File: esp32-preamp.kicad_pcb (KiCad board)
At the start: 2 copper layers, 126 x 68 mm, 46 parts, among them J1 INPUT 1, J10 LFE, J11 OUT, J2 INPUT 2, J3 AMP PWR, J5 VOLUME, J6 TSOP382, J7 SELECT, J8 POT MOTOR, J9 PWR IN, Q1 2N3904, Q2 2N3904, Q3 2N3904, U3 TSR0.5-2450, U4 TLV702475DBV, U5 TPS60402DBV, U6 ESP32 D1 Mini, U7 TPS72301DBV

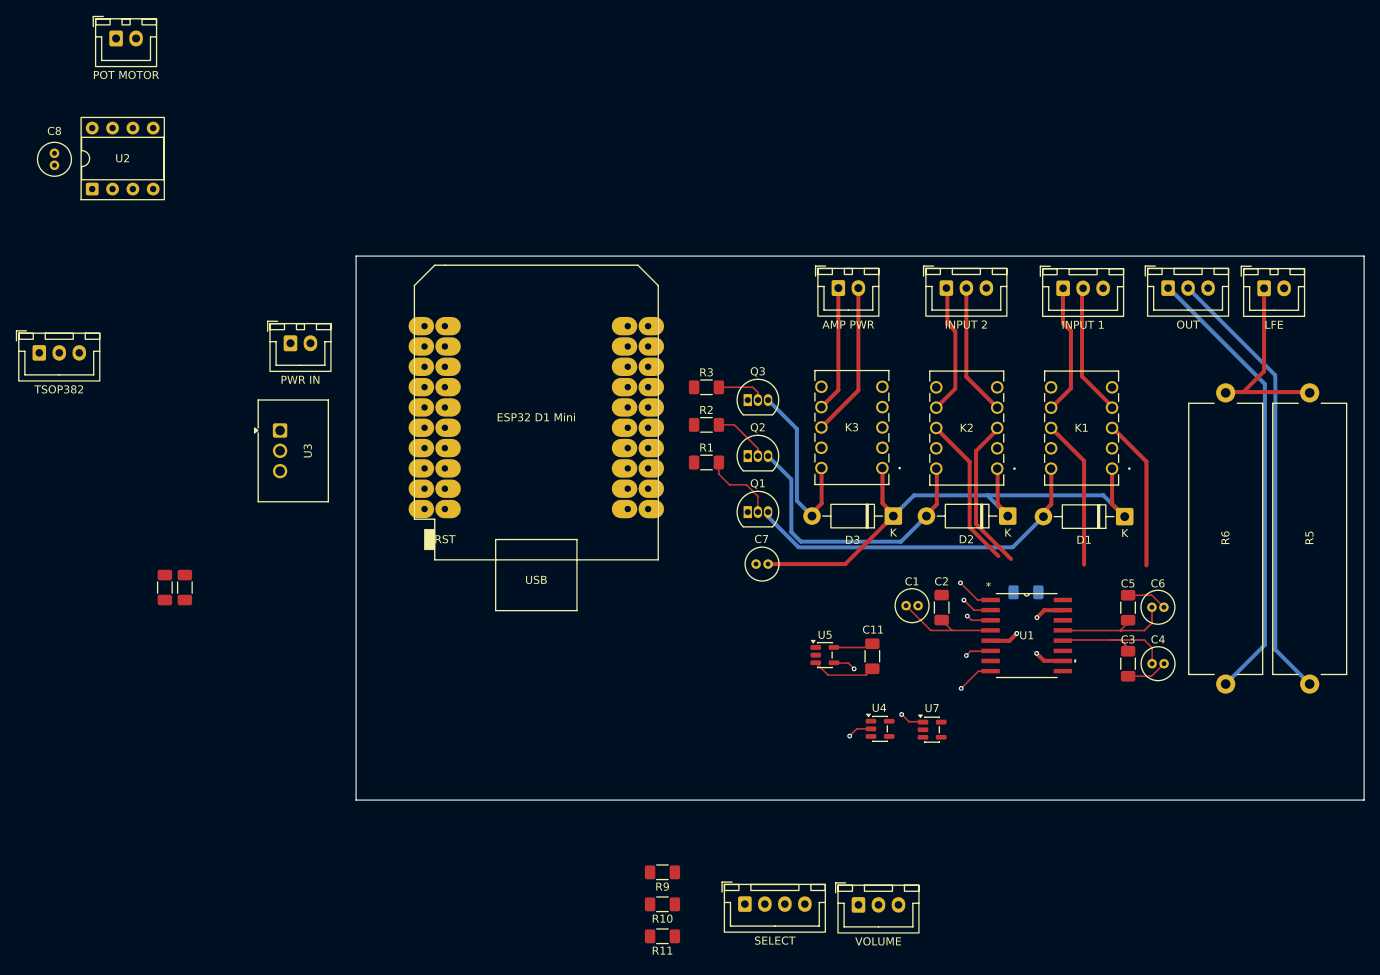
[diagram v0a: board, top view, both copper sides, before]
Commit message: More 5VA routing
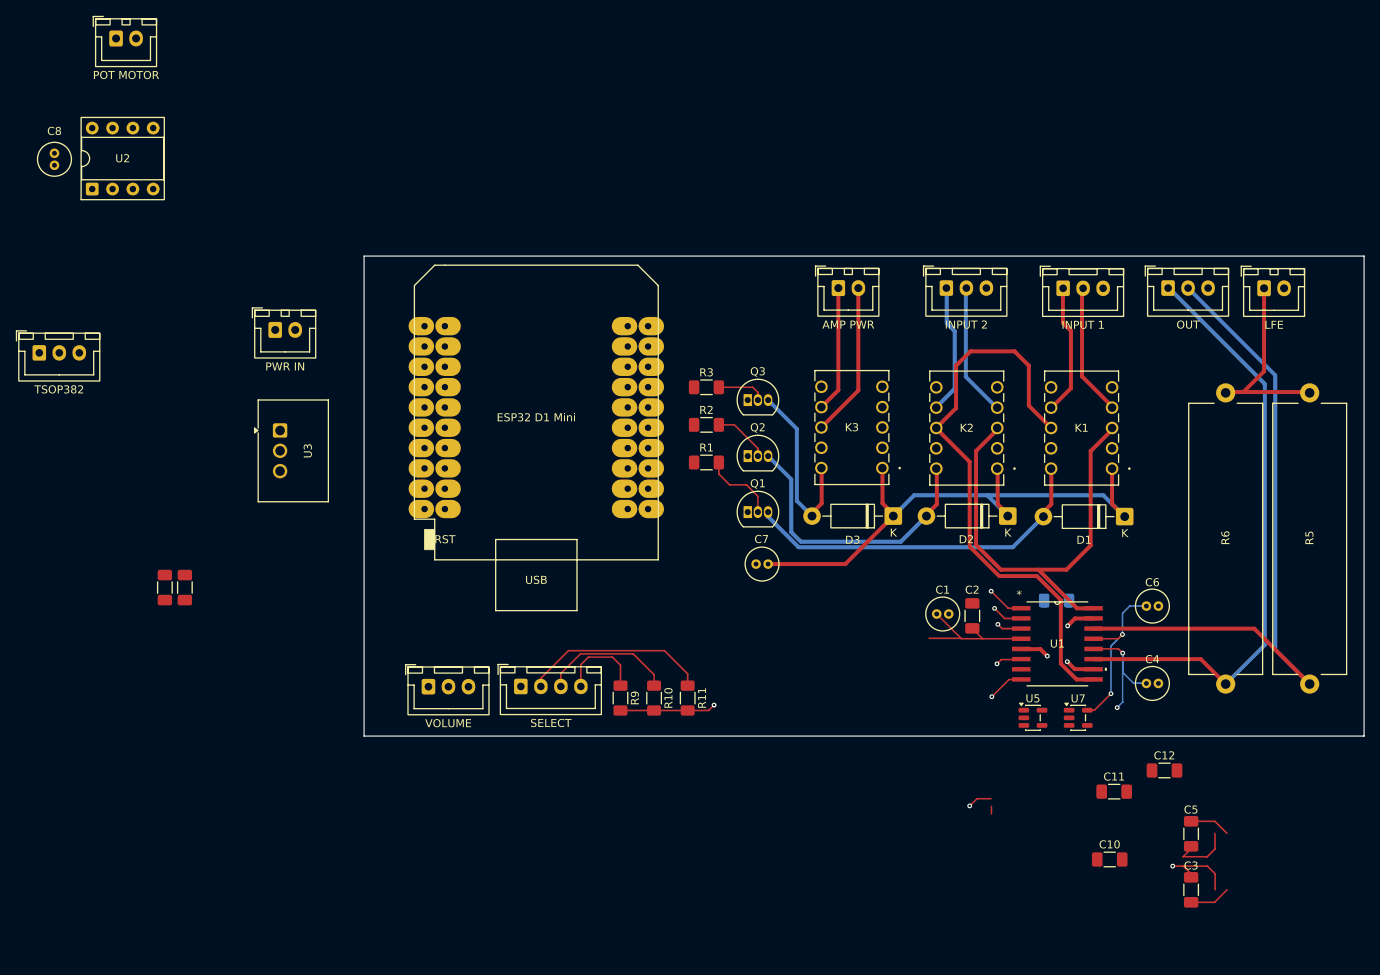
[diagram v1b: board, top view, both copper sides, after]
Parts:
- removed U4: TLV702475DBV, Package_TO_SOT_SMD:SOT-23-5
- added C10: 2.2uF, Capacitor_SMD:C_1206_3216Metric_Pad1.33x1.80mm_HandSolder, F.Cu at (164.2, 157.4)
- added C12: 2.2uF, Capacitor_SMD:C_1206_3216Metric_Pad1.33x1.80mm_HandSolder, F.Cu at (171.1, 146.3)
- moved J5 60.3 mm to (79.0, 135.8)
- moved J7 39.0 mm to (90.6, 135.8)
- moved C11 34.6 mm to (164.8, 148.9), turned to 0 degrees
- moved R11 29.9 mm to (111.5, 137.2), turned to -90 degrees
- moved C3 29.3 mm to (174.4, 161.2)
- moved C5 29.3 mm to (174.4, 154.2)
- moved U5 27.2 mm to (154.6, 139.7)
- moved R10 25.8 mm to (107.2, 137.2), turned to -90 degrees
- moved R9 22.4 mm to (103.0, 137.2), turned to -90 degrees
- moved U7 18.3 mm to (160.3, 139.7)
- moved C2 3.97 mm to (147.0, 127.0)
- moved C1 3.97 mm to (142.6, 126.7)
- moved R8 3.97 mm to (157.6, 125.1)
- moved U1 3.97 mm to (157.7, 130.5)
- moved C4 2.57 mm to (168.8, 135.4)
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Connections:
- C1 pad 1: +5VD -> +5VA
- C2 pad 1: +5VD -> +5VA
- C8 pad 1: +5VD -> +5VA
- K1 pad 3: IN_R -> IN_L
- K1 pad 8: IN_L -> IN_R
- K2 pad 3: IN_R -> IN_L
- K2 pad 8: IN_L -> IN_R
- U1 pad 4: +5VD -> +5VA
- U2 pad 2: +5VD -> +5VA
- U2 pad 3: +5VD -> +5VA
- U3 pad 3: +5VD -> +5VA
- U5 pad 2: +5VD -> +5VA
- U6 pad 35: +5VD -> +5VA
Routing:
- net IN_R: track 38.1 -> 72.0 mm
- net Net-(J11-Pin_2): track 55.8 -> 85.7 mm
- net +5VA: track 15.2 -> 42.7 mm, vias 0 -> 3
- net SELECT_1: track 0.00 -> 23.5 mm
- net IN_L: track 38.1 -> 57.2 mm
- net Net-(J11-Pin_1): track 56.6 -> 74.4 mm
- net SELECT_2: track 0.00 -> 16.7 mm
- net -5VA: track 14.4 -> 29.0 mm, vias 0 -> 2
- net +5VD: track 13.1 -> 0.00 mm
- net SELECT_3: track 0.00 -> 11.1 mm
- net Net-(U5-C_{FLY-}): track 8.04 -> 0.00 mm
- net GNDD: track 12.5 -> 18.6 mm, vias 4 -> 3
- net Net-(U5-C_{FLY+}): track 4.99 -> 0.00 mm
- net Net-(U5-OUT): track 0.00 -> 0.95 mm
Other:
- board size 126 x 68 mm -> 125 x 60 mm

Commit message: Update esp32-preamp.kicad_pcb
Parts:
- moved C12 24.2 mm to (165.5, 122.8), turned to 90 degrees
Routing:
- net GNDA: track 17.5 -> 7.26 mm
- net +5VA: track 42.7 -> 33.5 mm, vias 3 -> 2
- net -5VA: track 29.0 -> 25.2 mm
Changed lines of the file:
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@@
 	(footprint "Capacitor_SMD:C_1206_3216Metric_Pad1.33x1.80mm_HandSolder"
 		(layer "F.Cu")
-		(at 171.05 146.3)
+		(at 165.46 122.77 90)
 		(descr "Capacitor SMD 1206 (3216 Metric), square (rectangular) end terminal, IPC-7351 nominal with elongated pad for handsoldering. (Body size source: IPC-SM-782 page 76, https://www.pcb-3d.com/wordpress/wp-content/uploads/ipc-sm-782a_amendment_1_and_2.pdf)")
 		(tags "capacitor handsolder")
 		(property "Reference" "C12"
-			(at 0 -1.85 0)
+			(at 3.41 0.02 180)
 			(layer "F.SilkS")
 			(effects
@@
 		)
 		(property "Value" "2.2uF"
-			(at 0 1.85 0)
+			(at 0 1.85 90)
 			(layer "F.Fab")
 			(effects
@@
 		)
 		(property "Datasheet" ""
-			(at 0 0 0)
+			(at 0 0 90)
 			(layer "F.Fab")
 			(hide yes)
@@
 		)
 		(property "Description" "Unpolarized capacitor"
-			(at 0 0 0)
+			(at 0 0 90)
 			(layer "F.Fab")
 			(hide yes)
@@
 		)
 		(fp_text user "${REFERENCE}"
-			(at 0 0 0)
+			(at 0 0 90)
 			(layer "F.Fab")
 			(effects
@@
 		)
 		(pad "1" smd roundrect
-			(at -1.5625 0)
+			(at -1.5625 0 90)
 			(size 1.325 1.8)
 			(layers "F.Cu" "F.Mask" "F.Paste")
@@
 		)
 		(pad "2" smd roundrect
-			(at 1.5625 0)
+			(at 1.5625 0 90)
 			(size 1.325 1.8)
 			(layers "F.Cu" "F.Mask" "F.Paste")
@@
 	)
 	(segment
-		(start 172.08125 158.25635)
-		(end 173.40005 158.25635)
-		(width 0.2)
-		(layer "F.Cu")
-		(net "+5VA")
-	)
-	(segment
 		(start 142.5824 126.74)
 		(end 145.6212 129.7788)
@@
 	)
 	(segment
-		(start 174.40005 159.25635)
-		(end 173.40005 158.25635)
-		(width 0.2)
-		(layer "F.Cu")
-		(net "+5VA")
-	)
-	(segment
-		(start 173.40005 158.25635)
-		(end 176.41885 158.25635)
-		(width 0.2)
-		(layer "F.Cu")
-		(net "+5VA")
-	)
-	(segment
 		(start 152.56585 129.83)
 		(end 148.3224 129.83)
@@
 	)
 	(segment
-		(start 176.41885 158.25635)
-		(end 177.38125 159.21875)
-		(width 0.2)
-		(layer "F.Cu")
-		(net "+5VA")
-	)
-	(segment
 		(start 147.0324 128.54)
 		(end 148.3224 129.83)
@@
 	)
 	(segment
-		(start 177.38125 159.21875)
-		(end 177.38125 161.21875)
-		(width 0.2)
-		(layer "F.Cu")
-		(net "+5VA")
-	)
-	(segment
 		(start 165.3 131.1)
 		(end 162.92 131.1)
@@
 	)
 	(via
-		(at 172.08125 158.25635)
-		(size 0.6)
-		(drill 0.3)
-		(layers "F.Cu" "B.Cu")
-		(net "+5VA")
-	)
-	(via
 		(at 165.83 131.63)
 		(size 0.6)
@@
 	)
 	(segment
-		(start 177.31875 162.78125)
-		(end 174.38125 162.78125)
-		(width 0.2)
-		(layer "F.Cu")
-		(net "GNDA")
-	)
-	(segment
 		(start 162.1424 133.63)
 		(end 159.83 133.63)
@@
 	)
 	(segment
-		(start 177.35495 152.65625)
-		(end 178.86245 154.16375)
-		(width 0.2)
-		(layer "F.Cu")
-		(net "GNDA")
-	)
-	(segment
 		(start 162.1848 127.3)
 		(end 159.8724 127.3)
@@
 		(net "GNDA")
 	)
-	(segment
-		(start 174.38125 152.65625)
-		(end 177.35495 152.65625)
-		(width 0.2)
-		(layer "F.Cu")
-		(net "GNDA")
-	)
-	(segment
-		(start 178.88125 161.21875)
-		(end 177.31875 162.78125)
-		(width 0.2)
-		(layer "F.Cu")
-		(net "GNDA")
-	)
 	(via
 		(at 158.9424 128.23)
@@
 	)
 	(segment
-		(start 176.40005 157.08375)
-		(end 177.36245 156.12135)
-		(width 0.2)
-		(layer "F.Cu")
-		(net "-5VA")
-	)
-	(segment
-		(start 174.38125 156.08375)
-		(end 173.38125 157.08375)
+		(start 168.79 125.75)
+		(end 166.8775 125.75)
 		(width 0.2)
 		(layer "F.Cu")
@@
 	)
 	(segment
-		(start 161.4075 138.7675)
-		(end 162.2925 138.7675)
-		(width 0.2)
-		(layer "F.Cu")
-		(net "-5VA")
-	)
-	(segment
-		(start 176.38125 157.08375)
-		(end 176.40005 157.08375)
+		(start 166.8775 125.75)
+		(end 165.46 124.3325)
 		(width 0.2)
 		(layer "F.Cu")
@@
 	)
 	(segment
-		(start 177.36245 156.12135)
-		(end 177.36245 154.16375)
+		(start 161.4075 138.7675)
+		(end 162.2925 138.7675)
 		(width 0.2)
 		(layer "F.Cu")
@@
 		(width 0.2)
 		(layer "F.Cu")
-		(net "-5VA")
-	)
-	(segment
-		(start 173.38125 157.08375)
-		(end 176.38125 157.08375)
-		(width 0.2)
-		(layer "F.Cu")

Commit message: Tidy PGA2311 routing
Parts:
- moved C10 29.1 mm to (147.0, 133.9), turned to 90 degrees
- moved C11 19.4 mm to (147.8, 139.6)
- moved C12 16.9 mm to (166.6, 139.6), turned to 0 degrees
- moved C3 14.2 mm to (173.0, 147.1)
- moved C5 8.22 mm to (170.3, 147.1), turned to -90 degrees
- moved C4 0.79 mm to (168.4, 134.8)
- moved U5 0.77 mm to (154.1, 139.2), turned to 180 degrees
- moved C6 0.75 mm to (168.4, 125.1)
- moved U7 0.73 mm to (159.8, 139.1)
- moved U1 0.62 mm to (157.7, 129.9)
- moved C2 0.62 mm to (147.0, 126.4)
- moved R8 0.62 mm to (157.6, 124.4)
- moved C1 0.62 mm to (142.6, 126.1)
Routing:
- net Net-(U5-C_{FLY-}): track 0.00 -> 9.08 mm
- net Net-(U5-C_{FLY+}): track 0.00 -> 7.70 mm
- net +5VA: track 33.5 -> 40.6 mm
- net GNDD: track 18.6 -> 23.5 mm, vias 3 -> 4
- net Net-(U5-OUT): track 0.95 -> 4.45 mm
- net GNDA: track 7.26 -> 8.77 mm
- net IN_L: track 57.2 -> 56.5 mm
